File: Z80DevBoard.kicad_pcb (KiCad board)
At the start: 4 copper layers, 219 x 107.5 mm, 145 parts, among them SW1 WAIT, SW2 RESET, SW3 Z80BOOT, SW4 RPBOOT

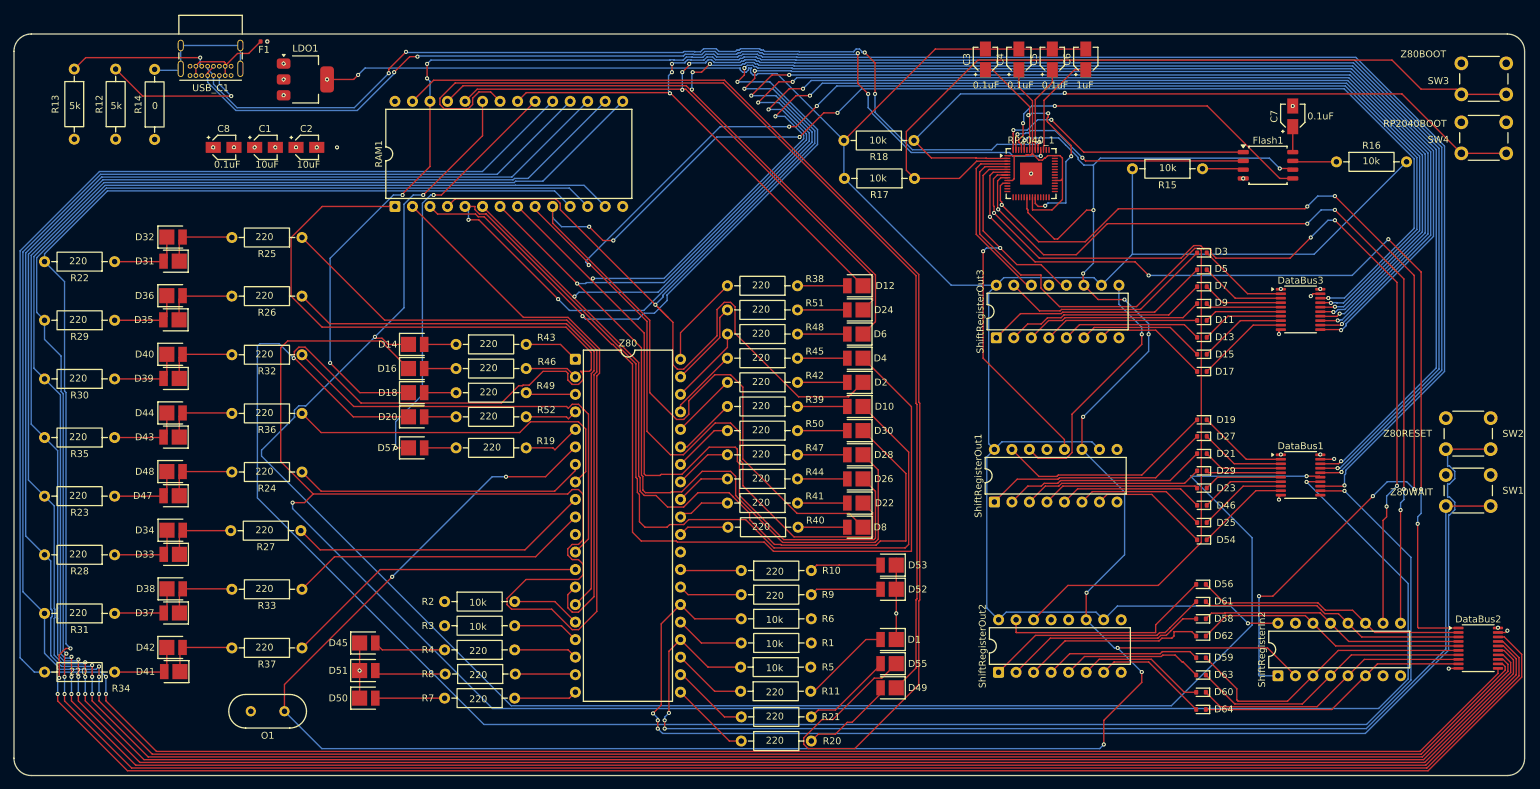
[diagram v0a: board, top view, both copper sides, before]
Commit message: Fixed vcc and 3v3 connections. Fixed GND layer. Removed old connections.
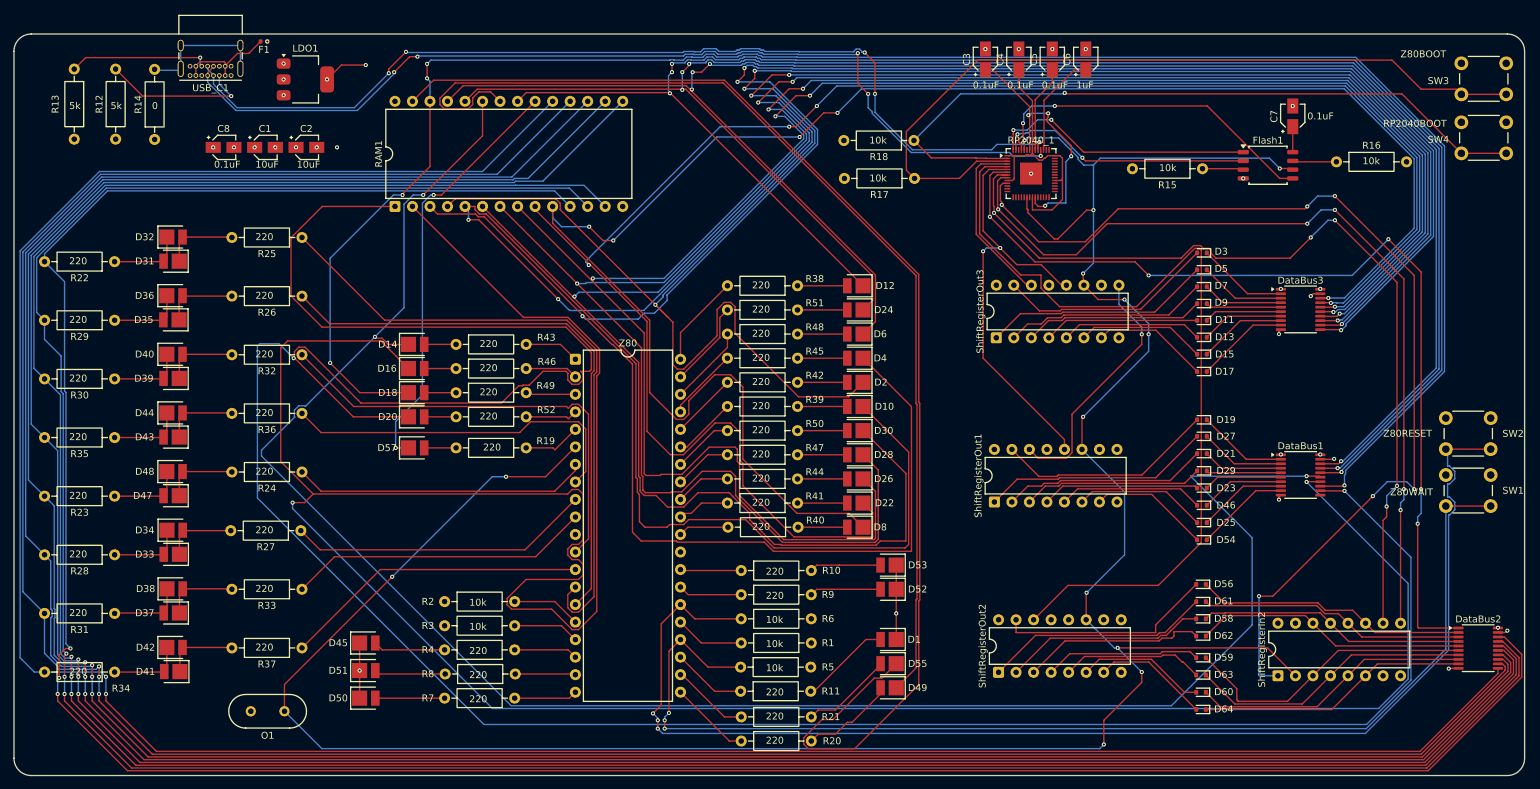
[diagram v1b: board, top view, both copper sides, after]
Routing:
- net Vdd_3v3: track 378.7 -> 457.0 mm, vias 7 -> 10

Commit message: Fixed the oscillators. Fixed the crystal. Fixed the connections between the RP2040 and the Flash. Updated README.
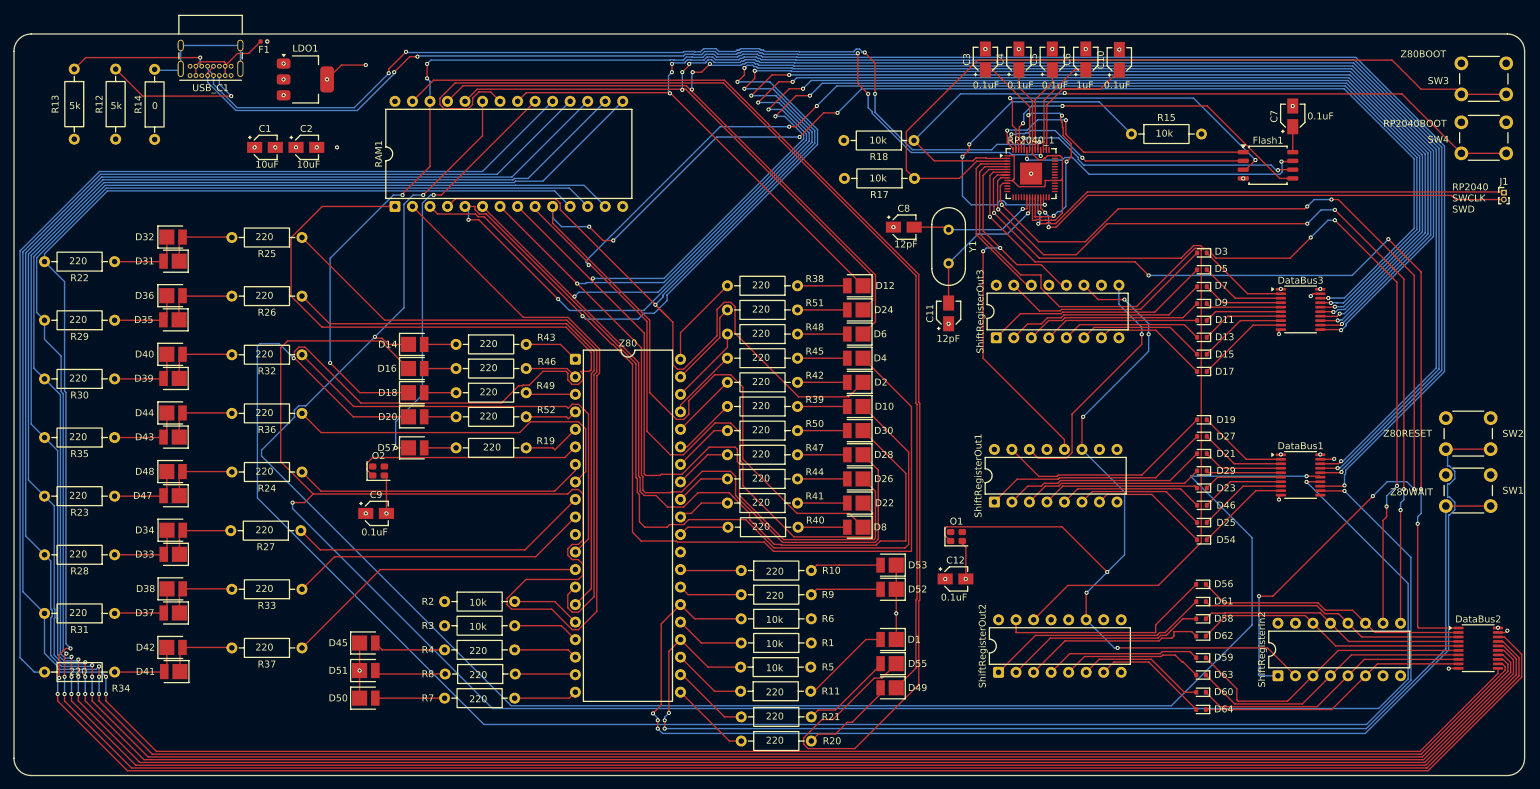
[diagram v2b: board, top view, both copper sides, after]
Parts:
- removed R16: 10k, Resistor_THT:R_Axial_DIN0207_L6.3mm_D2.5mm_P10.16mm_Horizontal
- added C10: 0.1uF, Capacitor_SMD:CP_Elec_3x5.3, F.Cu at (198.2, 42.2)
- added C11: 12pF, Capacitor_SMD:CP_Elec_3x5.3, F.Cu at (173.5, 79.0)
- added C12: 0.1uF, Capacitor_SMD:CP_Elec_3x5.3, F.Cu at (174.5, 117.5)
- added C9: 0.1uF, Capacitor_SMD:CP_Elec_3x5.3, F.Cu at (90.5, 108.0)
- added J1: Conn_01x02_MountingPin, Connector_PinHeader_1.00mm:PinHeader_1x02_P1.00mm_Vertical, F.Cu at (254.0, 61.5)
- added O2: 10KHz, Oscillator:Oscillator_SMD_SeikoEpson_SG210-4Pin_2.5x2.0mm, F.Cu at (90.8, 101.8)
- added Y1: Crystal, Crystal:Crystal_HC49-4H_Vertical, F.Cu at (173.5, 66.9)
- C8: value 0.1uF -> 12pF
- O1: value 6MHz -> 10KHz; footprint Crystal:Crystal_HC49-4H_Vertical -> Oscillator:Oscillator_SMD_SeikoEpson_SG210-4Pin_2.5x2.0mm
- moved O1 100.7 mm to (174.6, 111.3), turned to 0 degrees
- moved C8 99.3 mm to (167.0, 66.5)
- moved R15 11.5 mm to (200.0, 53.0), turned to 0 degrees
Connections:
- C8 pad 2: Vdd_3v3 -> RP2040_XIN
- Flash1 pad 3: FLASH-WP -> FLASH-WP-RP2040-QSPI_SD2
- Flash1 pad 6: CLOCK -> CLOCK_FLASH
- Flash1 pad 7: FLASH-HOLD/RESET -> FLASH-HOLD-RESRT-RP2040-QSPI_SD3
- O1 pad 1: CLOCK -> CLOCK_BUS
- R15 pad 1: FLASH-WP -> Vcc-RP2040-RUN
- RP2040_1 pad 20: CLOCK -> RP2040_XIN
- RP2040_1 pad 21: unconnected-(RP2040_1-XOUT-Pad21) -> RP2040_XOUT
- RP2040_1 pad 24: unconnected-(RP2040_1-SWCLK-Pad24) -> RP2040-SWCLK-PIN
- RP2040_1 pad 25: unconnected-(RP2040_1-SWD-Pad25) -> RP2040-SWD-PIN
- RP2040_1 pad 26: unconnected-(RP2040_1-RUN-Pad26) -> Vcc-RP2040-RUN
- RP2040_1 pad 44: unconnected-(RP2040_1-VREG_IN-Pad44) -> RP2040-VREG_IN
- RP2040_1 pad 51: unconnected-(RP2040_1-QSPI_SD3-Pad51) -> FLASH-HOLD-RESRT-RP2040-QSPI_SD3
- RP2040_1 pad 52: CLOCK -> CLOCK_FLASH
- RP2040_1 pad 54: unconnected-(RP2040_1-QSPI_SD2-Pad54) -> FLASH-WP-RP2040-QSPI_SD2
- ShiftRegisterIn2 pad 2: CLOCK -> CLOCK_BUS
- ShiftRegisterOut1 pad 11: CLOCK -> CLOCK_BUS
- ShiftRegisterOut2 pad 11: CLOCK -> CLOCK_BUS
- ShiftRegisterOut3 pad 11: CLOCK -> CLOCK_BUS
- Z80 pad 6: CLOCK -> CLOCK_Z80
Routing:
- net CLOCK: track 373.5 -> 0.00 mm, vias 13 -> 0
- net CLOCK_BUS: track 0.00 -> 125.9 mm, vias 0 -> 6
- net RP2040-SWCLK-PIN: track 0.00 -> 73.6 mm, vias 0 -> 2
- net RP2040-SWD-PIN: track 0.00 -> 73.0 mm, vias 0 -> 2
- net Vdd_3v3: track 457.0 -> 529.4 mm, vias 10 -> 12
- net Vcc-RP2040-RUN: track 0.00 -> 50.3 mm, vias 0 -> 3
- net FLASH-WP-RP2040-QSPI_SD2: track 0.00 -> 49.9 mm, vias 0 -> 2
- net CLOCK_FLASH: track 0.00 -> 43.3 mm, vias 0 -> 2
- net FLASH-HOLD-RESRT-RP2040-QSPI_SD3: track 0.00 -> 43.2 mm, vias 0 -> 2
- net CLOCK_Z80: track 0.00 -> 33.8 mm
- net RP2040_XOUT: track 0.00 -> 22.7 mm, vias 0 -> 1
- net Vcc: track 382.4 -> 361.8 mm
- net RP2040_XIN: track 0.00 -> 19.4 mm, vias 0 -> 1
- net RP2040-VREG_IN: track 0.00 -> 19.1 mm
- net RP2040-IOVDD: track 40.2 -> 48.1 mm
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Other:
- board text added: "12pF"
- board text added: "RP2040 SWCLK SWD"

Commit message: Added the manual clock for the Z80. Fixed all the components. Started fixing some connections.
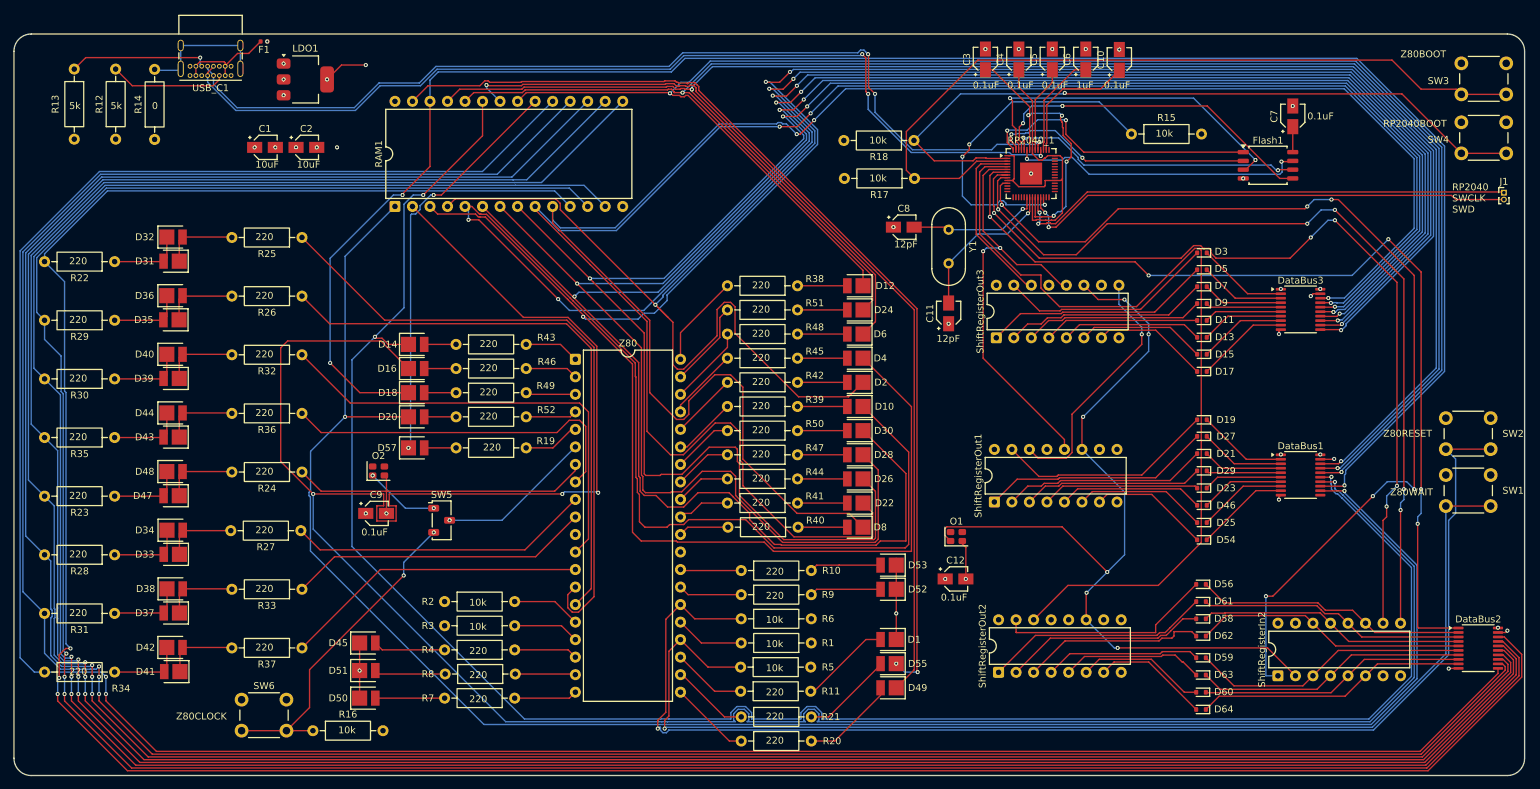
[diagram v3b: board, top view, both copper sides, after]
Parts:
- added R16: 10k, Resistor_THT:R_Axial_DIN0207_L6.3mm_D2.5mm_P10.16mm_Horizontal, F.Cu at (81.3, 139.5)
- added SW5: SW_Nidec_CAS-120A1, Button_Switch_SMD:Nidec_Copal_CAS-120A, F.Cu at (100.0, 109.0)
- added SW6: Z80_CLOCK, Button_Switch_THT:SW_PUSH_6mm_H7.3mm, F.Cu at (71.0, 135.0)
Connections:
- O2 pad 1: CLOCK_Z80 -> Net-(O2--)
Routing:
- net RAM-A14: track 394.6 -> 273.1 mm
- net Net-(SW5-A): track 0.00 -> 47.9 mm, vias 0 -> 2
- net RAM-A12: track 417.4 -> 374.9 mm, vias 2 -> 4
- net RAM-WE: track 185.5 -> 145.0 mm, vias 0 -> 2
- net Vdd_3v3: track 529.4 -> 566.7 mm
- net RAM-OE: track 154.6 -> 135.4 mm, vias 0 -> 1
- net Net-(O2--): track 0.00 -> 10.8 mm, vias 0 -> 2
- net CLOCK_Z80: track 33.8 -> 23.1 mm, vias 0 -> 1
- net RAM-A7: track 340.2 -> 330.7 mm
- net RAM-A6: track 279.9 -> 271.9 mm
- net RAM-A11: track 279.2 -> 285.8 mm
- net RAM-A5: track 338.7 -> 332.2 mm
- net RAM-A1: track 257.2 -> 263.1 mm, vias 4 -> 3
- net RAM-A4: track 302.0 -> 296.8 mm
- net USB-C-CC1: track 22.1 -> 17.0 mm, vias 1 -> 0
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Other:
- board text added: "Z80CLOCK"

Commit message: Fixed some connections. Recreated the gerber files.
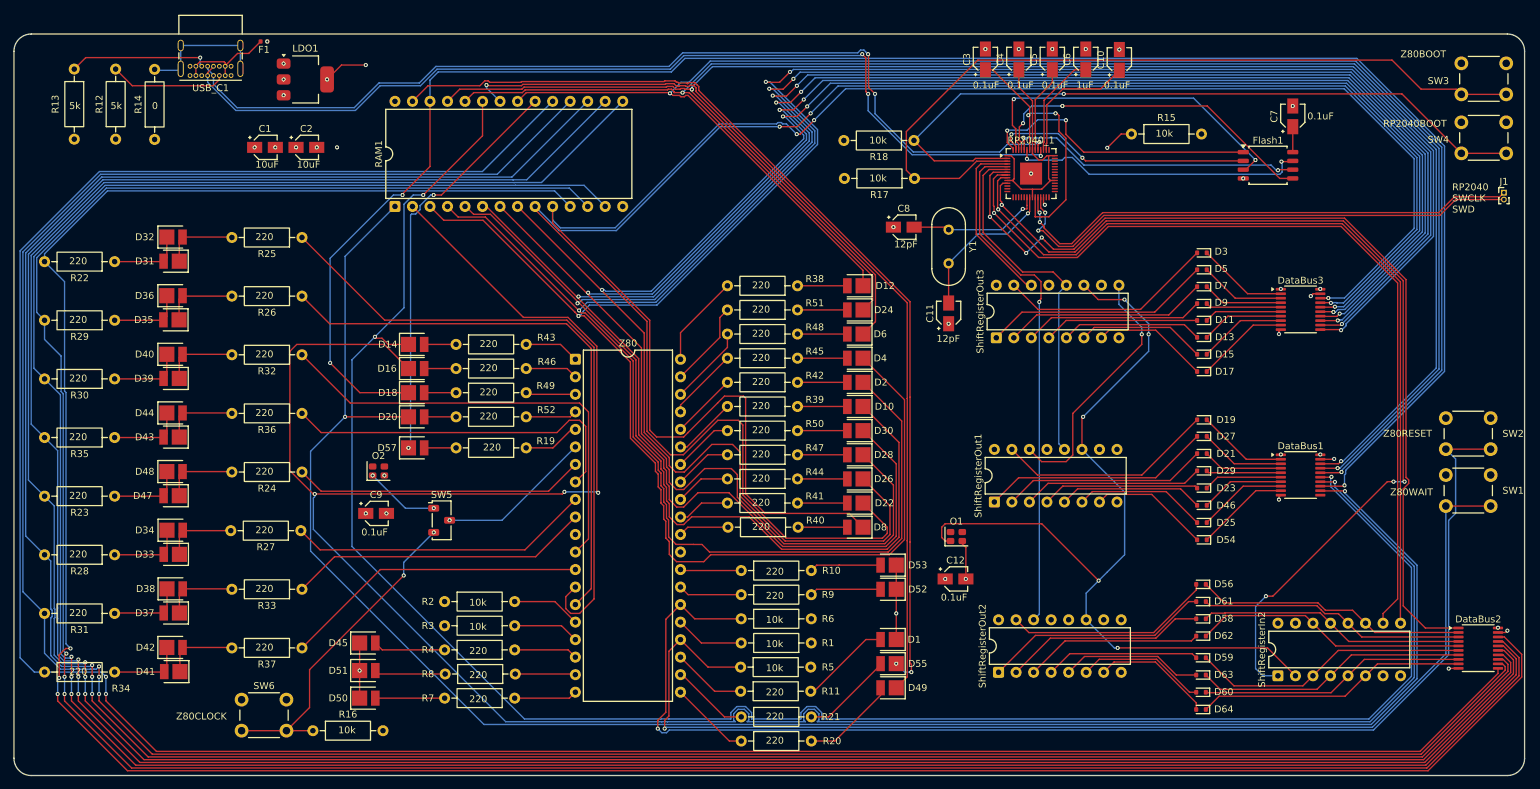
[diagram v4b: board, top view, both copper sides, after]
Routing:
- net RP2040-SH-GPIO3-SER: track 125.8 -> 74.5 mm, vias 0 -> 1
- net RAM-A6: track 271.9 -> 314.8 mm
- net Vcc-RP2040-RUN: track 50.3 -> 18.0 mm, vias 3 -> 2
- net RAM-A5: track 332.2 -> 304.3 mm, vias 5 -> 4
- net RAM-A12: track 374.9 -> 360.4 mm
- net RP2040-IOVDD: track 48.1 -> 33.9 mm
- net RP2040-SH-GPIO4-RCLK: track 63.5 -> 52.0 mm, vias 2 -> 0
- net Vdd_3v3: track 566.7 -> 561.8 mm, vias 12 -> 13
- net RAM-A1: track 263.1 -> 267.9 mm
- net RP2040-RWRAM-GPIO8-PL: track 146.2 -> 141.5 mm, vias 6 -> 4
- net RAM-A4: track 296.8 -> 292.0 mm
- net RP2040-SWD-PIN: track 73.0 -> 76.8 mm
- net RAM-A0: track 253.6 -> 257.2 mm
- net RAM-A7: track 330.7 -> 328.0 mm
- net RP2040-RWRAM-GPIO7-Q7: track 124.3 -> 121.7 mm, vias 5 -> 1
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
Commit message: Fixed a connection. Removed some useless connections.
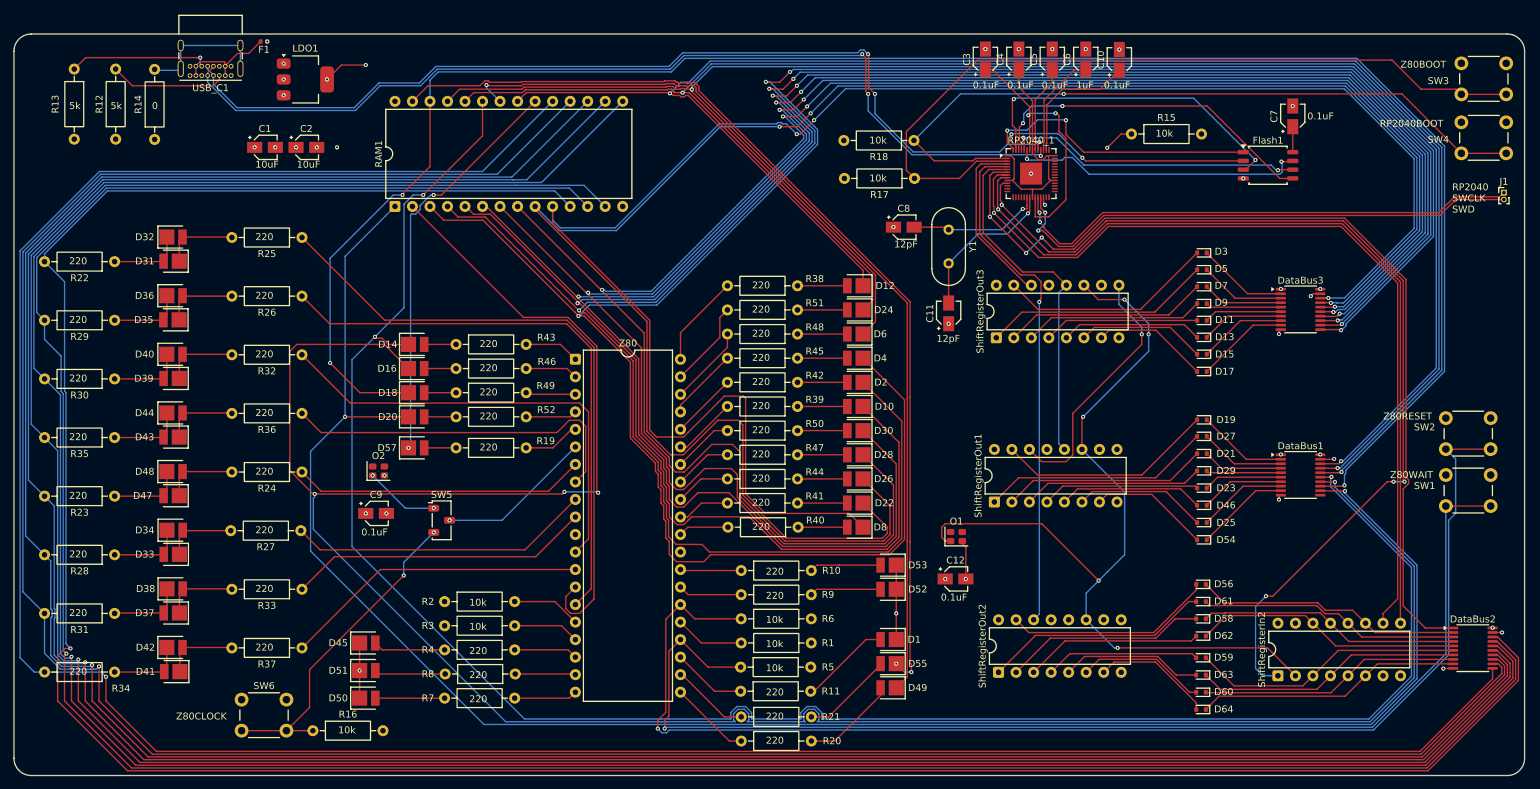
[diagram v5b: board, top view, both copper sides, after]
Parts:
- moved DataBus2 0.78 mm to (249.5, 127.5)
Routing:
- net Net-(D56-K): track 39.5 -> 38.7 mm
- net Net-(D64-K): track 39.4 -> 38.6 mm
- net Net-(D63-K): track 39.6 -> 38.8 mm
- net Net-(D60-K): track 38.7 -> 37.9 mm
- net Net-(D59-K): track 40.4 -> 39.7 mm
- net Net-(D62-K): track 39.7 -> 38.9 mm
- net Net-(D61-K): track 38.8 -> 38.0 mm
- net Net-(D58-K): track 38.7 -> 37.9 mm
- net RP2040-RWRAM-GPIO5-DIR: track 135.6 -> 134.8 mm
- net Vcc: track 361.1 -> 360.3 mm
- net RAM-Q7: track 372.5 -> 372.2 mm, vias 2 -> 1
- net RAM-Q3: track 385.8 -> 385.6 mm, vias 3 -> 1
- net RAM-Q0: track 378.3 -> 378.2 mm, vias 3 -> 1
- net RAM-Q2: track 380.3 -> 380.2 mm, vias 3 -> 1
- net RAM-Q1: track 378.4 -> 378.3 mm, vias 3 -> 1
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
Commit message: Fixed some connections.
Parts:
- moved USB_C1 0.16 mm to (69.5, 44.4)
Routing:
- net USB-C-CC2: track 20.3 -> 19.7 mm
- net Vdd_3v3: vias 13 -> 12
- net RP2040-RWRAM-GPIO8-PL: vias 4 -> 3
- net RP2040-RWRAM-GPIO7-Q7: vias 1 -> 0
- net RP2040-RWRAM-GPIO6-DS: vias 1 -> 0
- net RP2040-RWRAM-GPIO5-DIR: vias 3 -> 2
- net CLOCK_BUS: vias 5 -> 4
